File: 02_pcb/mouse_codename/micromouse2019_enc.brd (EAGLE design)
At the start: 5.9 x 11.1 mm, 7 parts, among them IC1 AS5047D

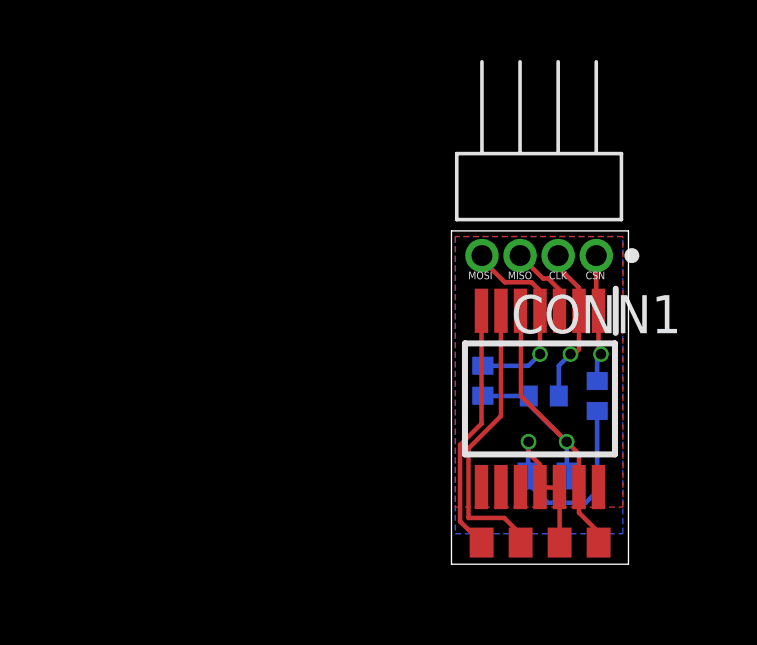
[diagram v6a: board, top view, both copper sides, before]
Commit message: BT_PORT_BASE updated
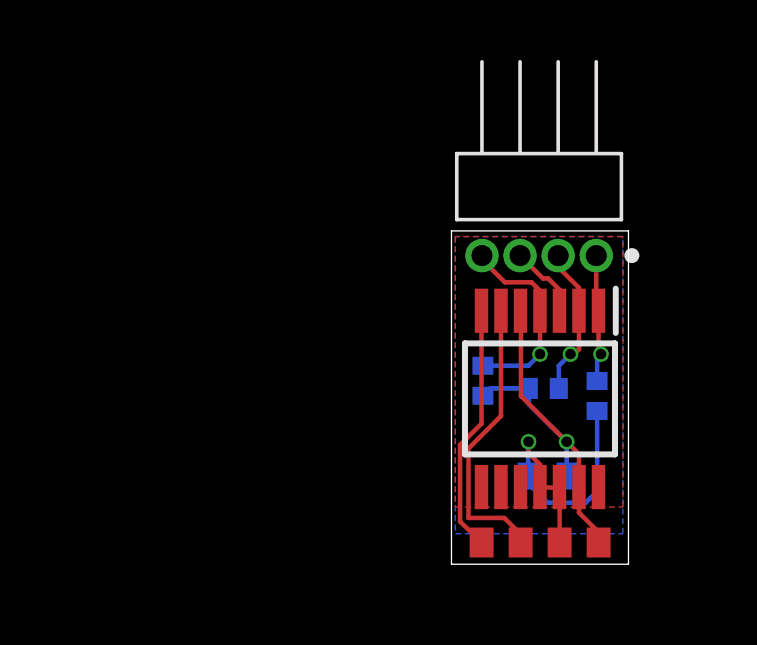
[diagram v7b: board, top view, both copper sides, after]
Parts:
- moved R2 0.25 mm to (3.08, 5.86)
